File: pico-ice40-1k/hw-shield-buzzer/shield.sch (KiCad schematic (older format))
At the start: 37 parts, among them J1 JACK_TRS_6PINS, P1 CONN_01X12, P2 CONN_01X04, SW1 SPST, SW2 SW_PUSH, U1 TLV320DAC3203, U2 LD39015M18R, U3 SSM2305

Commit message: Add librairies and upd sch
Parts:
- added C18: 0.1u, symbol C
- C16: renamed from 47u1; value C -> 47u
- C17: renamed from 47u2; value C -> 47u
- C5: value C_Small -> 1u
- R5, R6: renamed from 25k; value R -> 25k
- gave numbers to parts that had none: 5
- renumbered 100k to 100k1, 100k to 100k2
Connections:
- net +3V3: now also C18.1
- net GND: now also C18.2
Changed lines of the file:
@@
 $EndComp
 $Comp
-L GND #PWR8
+L GND #PWR5
 U 1 1 5731F16B
 P 1950 4900
-F 0 "#PWR8" H 1950 4650 50  0001 C CNN
+F 0 "#PWR5" H 1950 4650 50  0001 C CNN
 F 1 "GND" H 1950 4750 50  0000 C CNN
 F 2 "" H 1950 4900 50  0000 C CNN
@@
 $EndComp
 $Comp
-L GND #PWR25
+L GND #PWR27
 U 1 1 5732A695
 P 8650 3750
-F 0 "#PWR25" H 8650 3500 50  0001 C CNN
+F 0 "#PWR27" H 8650 3500 50  0001 C CNN
 F 1 "GND" H 8650 3600 50  0000 C CNN
 F 2 "" H 8650 3750 50  0000 C CNN
@@
 P 2400 6950
 F 0 "C5" H 2410 7020 50  0000 L CNN
-F 1 "C_Small" H 2050 6850 50  0000 L CNN
+F 1 "1u" H 2300 6850 50  0000 L CNN
 F 2 "" H 2400 6950 50  0000 C CNN
 F 3 "" H 2400 6950 50  0000 C CNN
@@
 $EndComp
 $Comp
-L GND #PWR6
+L GND #PWR7
 U 1 1 573304E6
 P 2400 7100
-F 0 "#PWR6" H 2400 6850 50  0001 C CNN
+F 0 "#PWR7" H 2400 6850 50  0001 C CNN
 F 1 "GND" H 2400 6950 50  0000 C CNN
 F 2 "" H 2400 7100 50  0000 C CNN
@@
 $EndComp
 $Comp
-L GND #PWR24
+L GND #PWR25
 U 1 1 57337161
 P 7550 5400
-F 0 "#PWR24" H 7550 5150 50  0001 C CNN
+F 0 "#PWR25" H 7550 5150 50  0001 C CNN
 F 1 "GND" H 7550 5250 50  0000 C CNN
 F 2 "" H 7550 5400 50  0000 C CNN
@@
 $EndComp
 $Comp
-L GND #PWR5
+L GND #PWR6
 U 1 1 57334BD9
 P 2150 2400
-F 0 "#PWR5" H 2150 2150 50  0001 C CNN
+F 0 "#PWR6" H 2150 2150 50  0001 C CNN
 F 1 "GND" H 2150 2250 50  0000 C CNN
 F 2 "" H 2150 2400 50  0000 C CNN
@@
 $EndComp
 $Comp
-L GND #PWR7
+L GND #PWR8
 U 1 1 573668D4
 P 2650 7550
-F 0 "#PWR7" H 2650 7300 50  0001 C CNN
+F 0 "#PWR8" H 2650 7300 50  0001 C CNN
 F 1 "GND" H 2650 7400 50  0000 C CNN
 F 2 "" H 2650 7550 50  0000 C CNN
@@
 $EndComp
 $Comp
-L C 47u1
+L C C16
 U 1 1 5735FB8C
 P 8900 4100
-F 0 "47u1" H 8925 4200 50  0000 L CNN
-F 1 "C" H 8925 4000 50  0000 L CNN
+F 0 "C16" H 8925 4200 50  0000 L CNN
+F 1 "47u" H 8925 4000 50  0000 L CNN
 F 2 "" H 8938 3950 50  0000 C CNN
 F 3 "" H 8900 4100 50  0000 C CNN
@@
 $EndComp
 $Comp
-L C 47u2
+L C C17
 U 1 1 5735FC9E
 P 8900 4350
-F 0 "47u2" H 8925 4450 50  0000 L CNN
-F 1 "C" H 8925 4250 50  0000 L CNN
+F 0 "C17" H 8925 4450 50  0000 L CNN
+F 1 "47u" H 8925 4250 50  0000 L CNN
 F 2 "" H 8938 4200 50  0000 C CNN
 F 3 "" H 8900 4350 50  0000 C CNN
@@
 $EndComp
 $Comp
-L C C?
+L C C14
 U 1 1 57363E8E
 P 1950 4600
-F 0 "C?" V 2050 4700 50  0000 L CNN
+F 0 "C14" V 2050 4700 50  0000 L CNN
 F 1 "1u" V 1900 4450 50  0000 L CNN
 F 2 "" H 1988 4450 50  0000 C CNN
@@
 $EndComp
 $Comp
-L R R?
+L R R3
 U 1 1 573665D1
 P 6350 900
-F 0 "R?" V 6430 900 50  0000 C CNN
+F 0 "R3" V 6430 900 50  0000 C CNN
 F 1 "R" V 6350 900 50  0000 C CNN
 F 2 "" V 6280 900 50  0000 C CNN
@@
 $EndComp
 $Comp
-L LED D?
+L LED D1
 U 1 1 57366632
 P 6850 900
-F 0 "D?" H 6850 1000 50  0000 C CNN
+F 0 "D1" H 6850 1000 50  0000 C CNN
 F 1 "LED" H 6850 800 50  0000 C CNN
 F 2 "" H 6850 900 50  0000 C CNN
@@
 $EndComp
 $Comp
-L GND #PWR?
+L GND #PWR24
 U 1 1 573666FB
 P 7400 950
-F 0 "#PWR?" H 7400 700 50  0001 C CNN
+F 0 "#PWR24" H 7400 700 50  0001 C CNN
 F 1 "GND" H 7400 800 50  0000 C CNN
 F 2 "" H 7400 950 50  0000 C CNN
@@
 $EndComp
 $Comp
-L SSM2305 U?
+L SSM2305 U4
 U 1 1 57367DB5
 P 7700 1200
-F 0 "U?" H 9650 650 60  0000 C CNN
+F 0 "U4" H 9650 650 60  0000 C CNN
 F 1 "SSM2305" H 9800 550 60  0000 C CNN
 F 2 "" H 9850 -450 60  0000 C CNN
@@
 $EndComp
 $Comp
-L C C?
+L C C15
 U 1 1 57369383
 P 8100 1050
-F 0 "C?" V 8200 1150 50  0000 L CNN
+F 0 "C15" V 8200 1150 50  0000 L CNN
 F 1 "1u" H 8000 950 50  0000 L CNN
 F 2 "" H 8138 900 50  0000 C CNN
@@
 $EndComp
 $Comp
-L GND #PWR?
+L GND #PWR26
 U 1 1 57369389
 P 8100 1250
-F 0 "#PWR?" H 8100 1000 50  0001 C CNN
+F 0 "#PWR26" H 8100 1000 50  0001 C CNN
 F 1 "GND" H 8100 1100 50  0000 C CNN
 F 2 "" H 8100 1250 50  0000 C CNN
@@
 $EndComp
 $Comp
-L +3.3V #PWR?
+L +3.3V #PWR28
 U 1 1 5736A304
 P 9550 1300
-F 0 "#PWR?" H 9550 1150 50  0001 C CNN
+F 0 "#PWR28" H 9550 1150 50  0001 C CNN
 F 1 "+3.3V" H 9550 1440 50  0000 C CNN
 F 2 "" H 9550 1300 50  0000 C CNN
@@
 $EndComp
 $Comp
-L GND #PWR?
+L GND #PWR29
 U 1 1 5736A3EA
 P 9550 2350
-F 0 "#PWR?" H 9550 2100 50  0001 C CNN
+F 0 "#PWR29" H 9550 2100 50  0001 C CNN
 F 1 "GND" H 9550 2200 50  0000 C CNN
 F 2 "" H 9550 2350 50  0000 C CNN
@@
 $EndComp
 $Comp
-L POT 100k
+L POT 100k1
 U 1 1 5736BB3E
 P 7900 1800
-F 0 "100k" H 7900 1700 50  0000 C CNN
+F 0 "100k1" H 7900 1700 50  0000 C CNN
 F 1 "POT" H 7900 1800 50  0000 C CNN
 F 2 "" H 7900 1800 50  0000 C CNN
@@
 $EndComp
 $Comp
-L POT 100k
+L POT 100k2
 U 1 1 5736CFF7
 P 7900 2000
-F 0 "100k" H 7900 1900 50  0000 C CNN
+F 0 "100k2" H 7900 1900 50  0000 C CNN
 F 1 "POT" H 7900 2000 50  0000 C CNN
 F 2 "" H 7900 2000 50  0000 C CNN
@@
 $EndComp
 $Comp
-L R 25k
+L R R5
 U 1 1 5736EB35
 P 8550 1850
-F 0 "25k" V 8630 1850 50  0000 C CNN
-F 1 "R" V 8550 1850 50  0000 C CNN
+F 0 "R5" V 8630 1850 50  0000 C CNN
+F 1 "25k" V 8550 1850 50  0000 C CNN
 F 2 "" V 8480 1850 50  0000 C CNN
 F 3 "" H 8550 1850 50  0000 C CNN
@@
 $EndComp
 $Comp
-L R 25k
+L R R6
 U 1 1 5736EBA4
 P 8550 2000
-F 0 "25k" V 8630 2000 50  0000 C CNN
-F 1 "R" V 8550 2000 50  0000 C CNN
+F 0 "R6" V 8630 2000 50  0000 C CNN
+F 1 "25k" V 8550 2000 50  0000 C CNN
 F 2 "" V 8480 2000 50  0000 C CNN
 F 3 "" H 8550 2000 50  0000 C CNN
@@
 	7550 5350 7550 5400
 Wire Wire Line
-	1350 1300 2500 1300
+	1350 1300 2750 1300
 Wire Wire Line
 	1000 1950 1700 1950
@@
 	2900 2350 2900 2400
 Wire Wire Line
-	1350 900  2500 900
+	1350 900  2750 900
 Wire Wire Line
 	6600 1450 6600 1250
@@
 	8300 1850 8300 1800
 NoConn ~ 8900 1800
+$Comp
+L C C18
+U 1 1 5736714E
+P 2750 1100
+F 0 "C18" H 2775 1200 50  0000 L CNN
+F 1 "0.1u" H 2775 1000 50  0000 L CNN
+F 2 "" H 2788 950 50  0000 C CNN
+F 3 "" H 2750 1100 50  0000 C CNN
+	1    2750 1100
+	1    0    0    -1
+$EndComp
+Wire Wire Line
+	2750 900  2750 950
+Connection ~ 2500 900
+Wire Wire Line
+	2750 1300 2750 1250
+Connection ~ 2500 1300
 $EndSCHEMATC

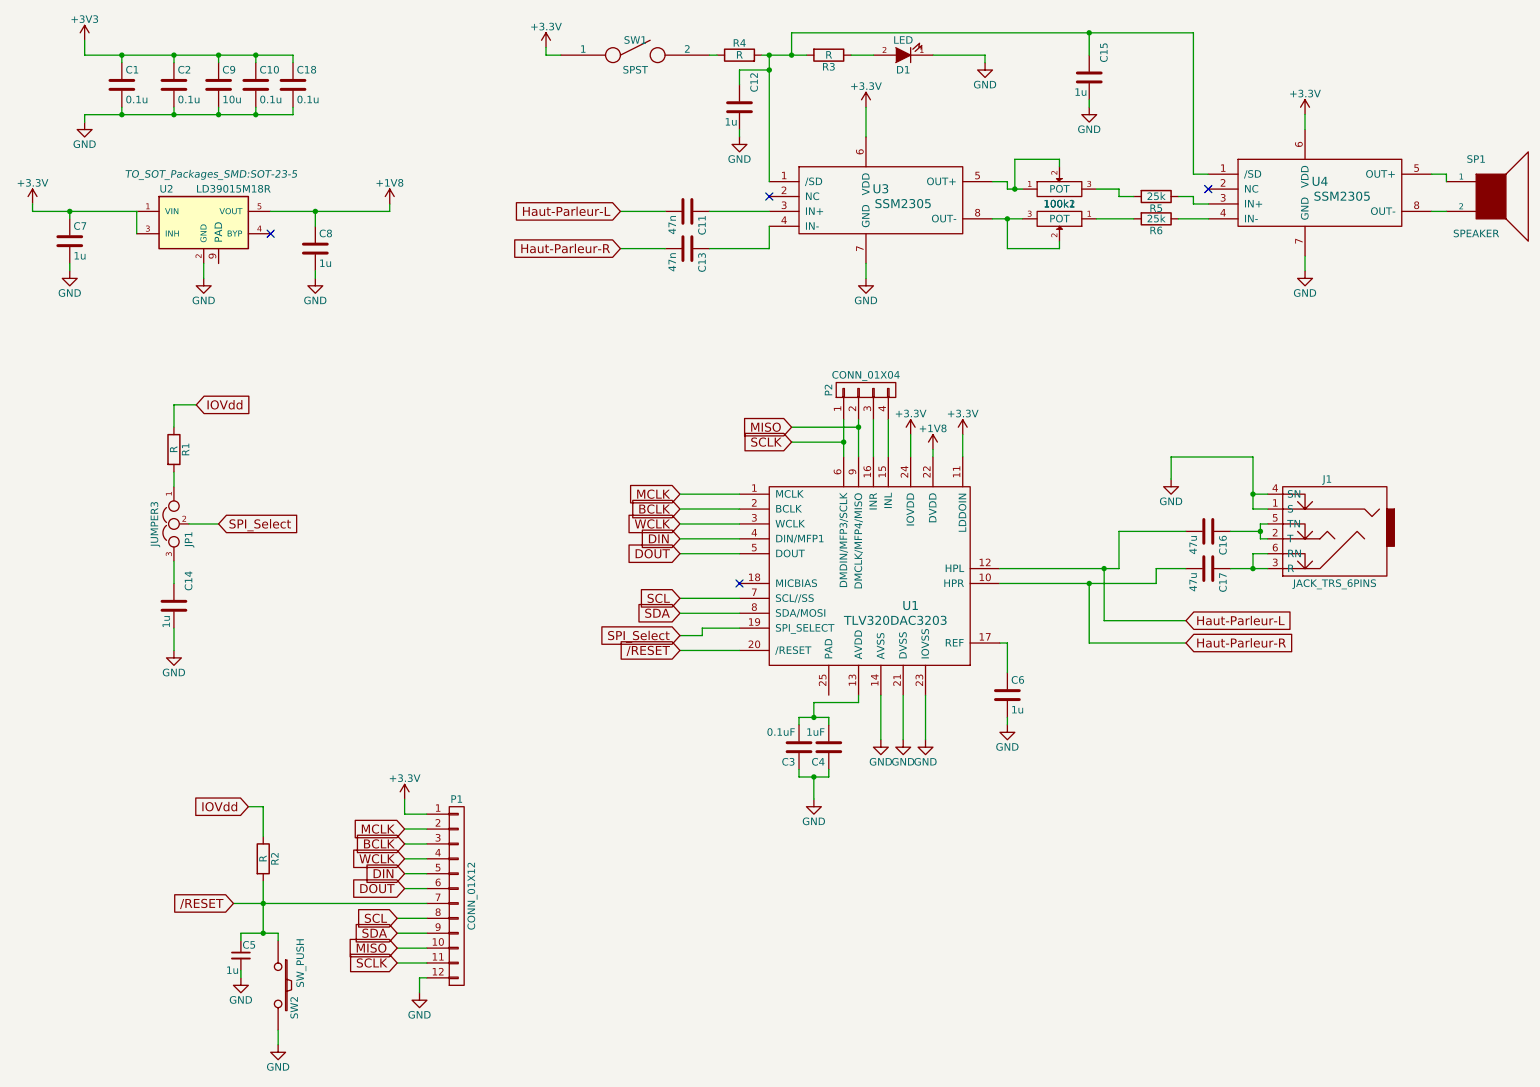
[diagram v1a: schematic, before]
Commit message: new schema and PCB with lib for jack connector
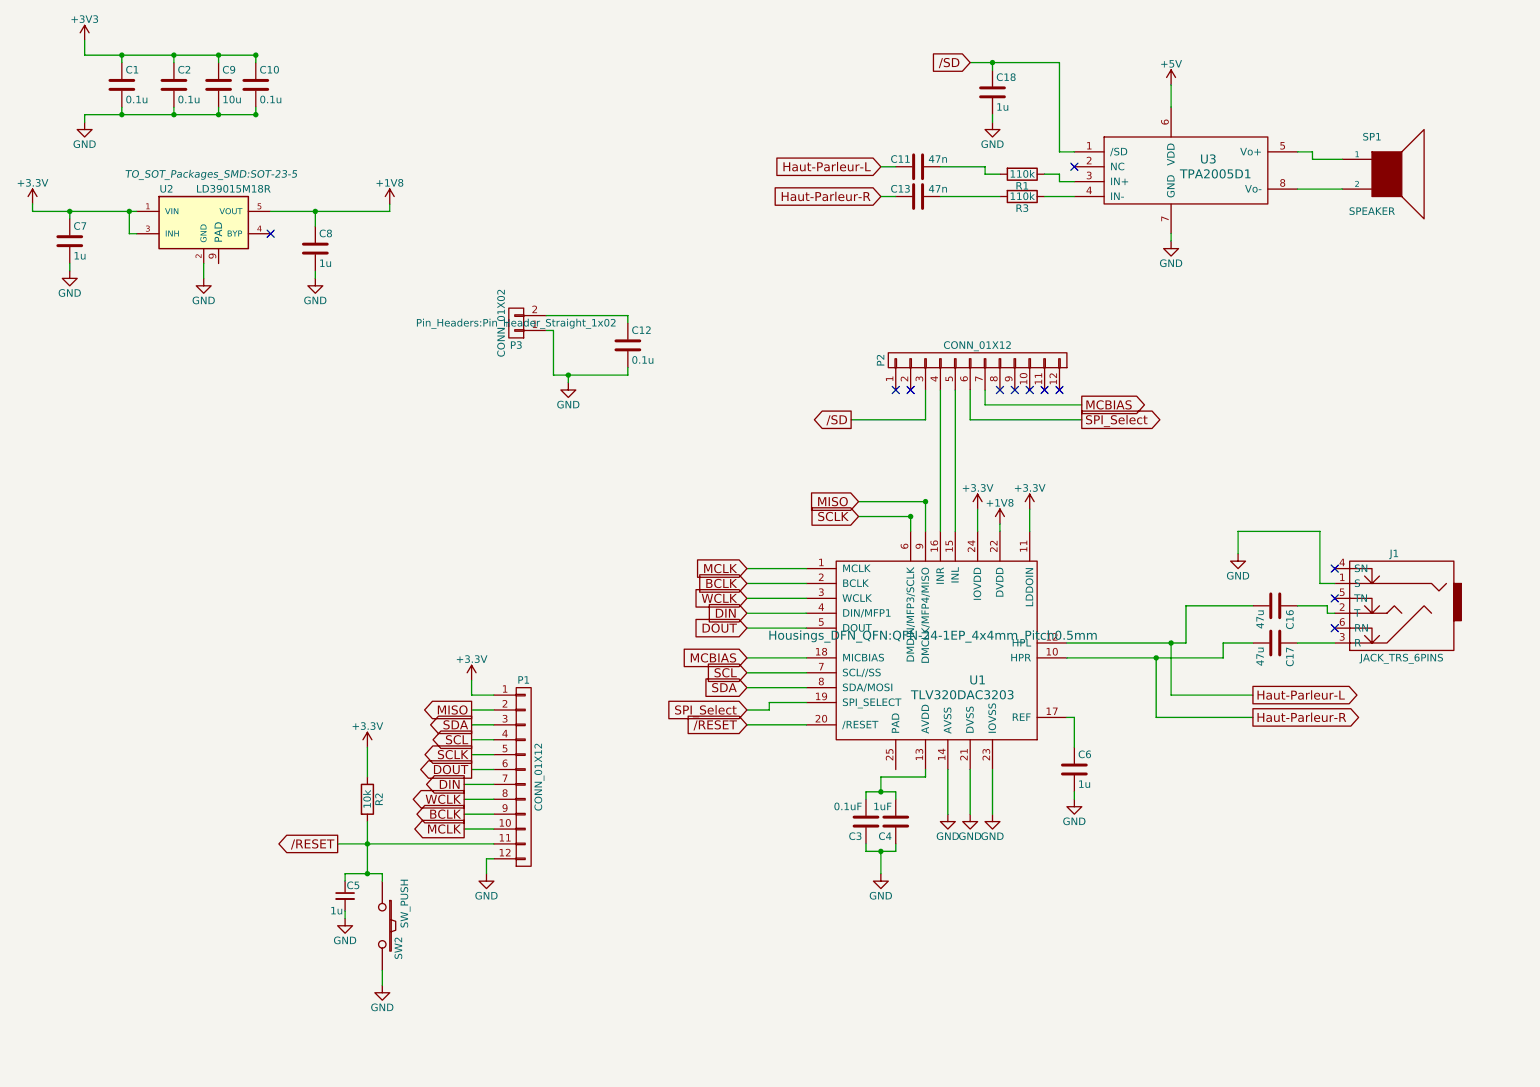
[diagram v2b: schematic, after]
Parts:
- removed 100k1, 100k2: POT, symbol POT
- removed C14, C15: 1u, symbol C
- removed D1: LED, symbol LED
- removed JP1: JUMPER3, symbol JUMPER3
- removed P2: CONN_01X04, symbol CONN_01X04
- removed R4: R, symbol R
- removed R5, R6: 25k, symbol R
- removed SW1: SPST, symbol SPST
- removed U3, U4: SSM2305, symbol SSM2305
- added P2: CONN_01X12, Pin_Headers:Pin_Header_Straight_1x12, symbol CONN_01X12
- added P3: CONN_01X02, Pin_Headers:Pin_Header_Straight_1x02, symbol CONN_01X02
- added U3: TPA2005D1, Housings_SSOP:MSOP-8-1EP_3x3mm_Pitch0.65mm, symbol TPA2005D1
- C1, C11, C13, C2, C3: footprint (none) -> Capacitors_SMD:C_0603
- C10, C16, C17, C4, C5, C6, C7, C8, C9: footprint (none) -> Capacitors_SMD:C_0805
- C12: value 1u -> 0.1u; footprint (none) -> Capacitors_SMD:C_0805
- C18: value 0.1u -> 1u; footprint (none) -> Capacitors_SMD:C_0603
- J1: footprint (none) -> shield_foorprint:Jack Cliff FC68131
- P1: footprint (none) -> Pin_Headers:Pin_Header_Straight_1x12
- R1, R3: value R -> 110k; footprint (none) -> Resistors_SMD:R_0603
- R2: value R -> 10k; footprint (none) -> Resistors_SMD:R_0603
- SP1: footprint (none) -> Buzzers_Beepers:BUZZER
- SW2: footprint (none) -> Buttons_Switches_ThroughHole:SW_PUSH_SMALL
- U1: footprint (none) -> Housings_DFN_QFN:QFN-24-1EP_4x4mm_Pitch0.5mm; Fabricant  (none) -> TEXAS INSTRUMENTS; Ref Farnell (none) -> 2144241; Reference Fabricant (none) -> TLV320DAC3203IRGET
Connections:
- net +3V3: now also R2.1; no longer C18.1
- net /RESET: now also P1.11 (P11); no longer P1.7 (P7)
- net BCLK: now also P1.9 (P9); no longer P1.3 (P3)
- net DIN: now also P1.7 (P7); no longer P1.5 (P5)
- net GND: now also P3.1 (P1), U3.7 (GND); no longer J1.4 (SN)
- net Haut-Parleur-L: now also C11.1; no longer C11.2
- net Haut-Parleur-R: now also C13.1; no longer C13.2
- net MCLK: now also P1.10 (P10); no longer P1.2 (P2)
- net MISO: now also P1.2 (P2); no longer P1.10 (P10)
- net SCL: now also P1.4 (P4); no longer P1.8 (P8)
- net SCLK: now also P1.5 (P5); no longer P1.11 (P11)
- net SDA: now also P1.3 (P3); no longer P1.9 (P9)
- net SPI_Select: now also P2.6 (P6)
- net WCLK: now also P1.8 (P8); no longer P1.4 (P4)
- net at U1.15 (INL): now also P2.5 (P5)
- net at U1.16 (INR): now also P2.4 (P4)
- net MCBIAS: now reaches U1.18 (MICBIAS)
- net MCBIAS: now also P2.7 (P7)
- net at R1.2: now also C11.2
- net at C16.1, J1.2 (T): no longer J1.5 (TN)
- net at C17.1, J1.3 (R): no longer J1.6 (RN)
- net at SP1.1: now also U3.5 (Vo+)
- net at SP1.2: now also U3.8 (Vo-)
- net at R3.2: now also C13.2; no longer C12.1
- net at R3.1: now also U3.4 (IN-)
- net IOVdd: no longer names the net of R1.1
- net IOVdd: now also U3.3 (IN+); no longer R2.1
- new net: C12.1, P3.2 (P2)
- new net +5V: U3.6 (VDD)
- new net /SD: C18.1, P2.3 (P3), U3.1 (/SD)
- no-connect marks 4 -> 12
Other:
- moved on the sheet: C16, C17, C18, C3, C4, C5, C6, J1, P1, R2, SP1, SW2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

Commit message: Modif sch and pcb
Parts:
- removed C2: 0.1u, Capacitors_SMD:C_0603, symbol C
- C1, C11, C13, C18, C3: footprint Capacitors_SMD:C_0603 -> Capacitors_SMD:C_0805
- J1: Fabricant (none) -> CLIFF ELECTRONIC COMPONENTS; Ref Fabricant (none) -> FC68131; Ref Farnell (none) -> 2518188
- U2: Fabrcant (none) -> STMICROELECTRONICS; Ref Farnell (none) -> 2311332; ref Fabricant (none) -> LD39015M18R
- U3: Fabricant (none) -> TEXAS INSTRUMENTS; Ref Fabricant (none) -> TPA2005D1DGN; Ref Farnell (none) -> 2075395
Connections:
- net +5V: now also C12.1, P3.2 (P2)
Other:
- moved on the sheet: C10, C9
